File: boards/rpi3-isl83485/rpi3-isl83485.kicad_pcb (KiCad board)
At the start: 2 copper layers, 24.8 x 15.2 mm, 9 parts, among them J1 RPi, J2 JST-GH, U1 ISL83485

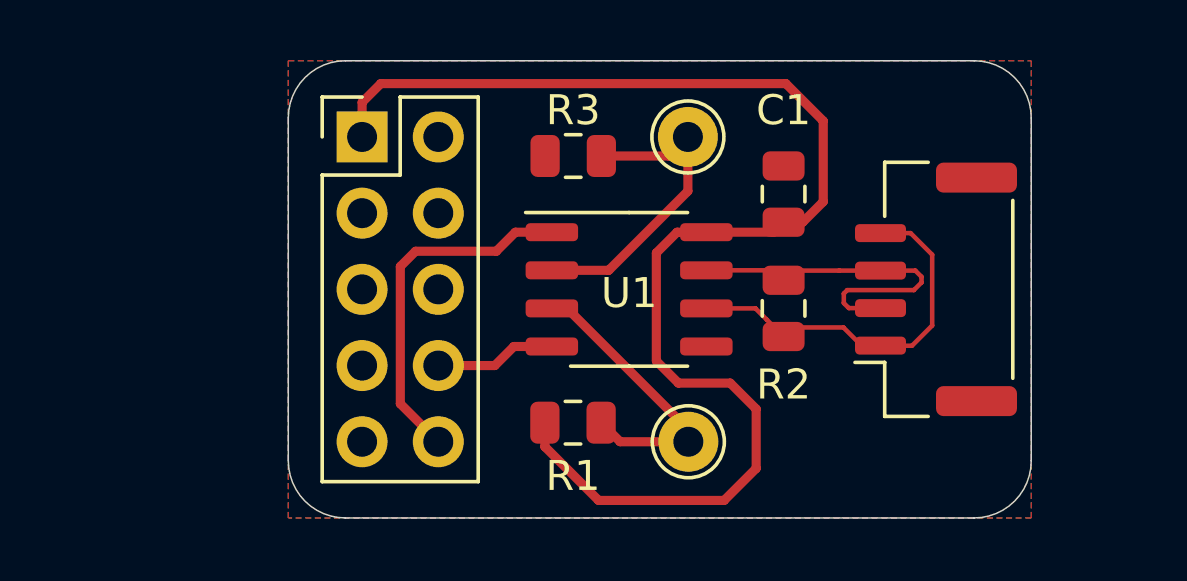
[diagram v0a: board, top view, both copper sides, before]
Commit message: No longer interested in ISL83488.
Layout for ICE40HX8K-BG121 -- just need power.
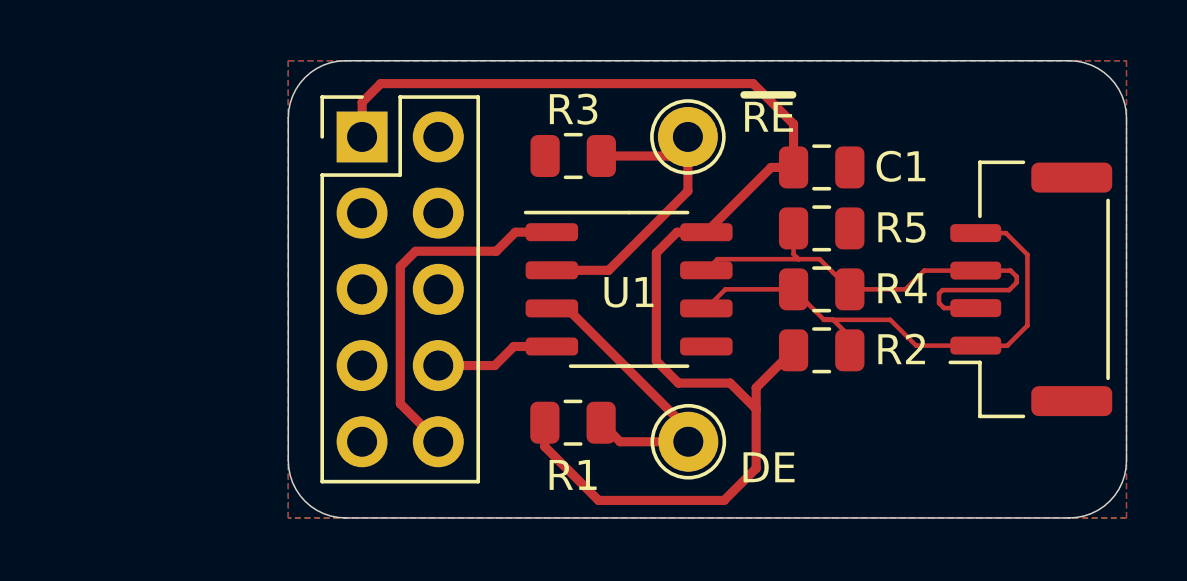
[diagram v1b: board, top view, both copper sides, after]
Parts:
- added R4: Rt, Resistor_SMD:R_0805_2012Metric, F.Cu at (34.3, 22.9)
- added R5: Rb, Resistor_SMD:R_0805_2012Metric, F.Cu at (34.3, 20.8)
- R2: value 100R -> Rb
- moved J2 3.17 mm to (41.3, 22.9)
- moved R2 1.89 mm to (34.3, 24.9), turned to 0 degrees
- moved C1 1.55 mm to (34.3, 18.8), turned to 0 degrees
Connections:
- R2 pad 1: /DS- -> +3V3
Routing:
- net /DS+: track 13.0 -> 18.0 mm
- net /DS-: track 12.1 -> 16.9 mm
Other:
- board size 24.8 x 15.2 mm -> 27.9 x 15.2 mm
- board text added: "DE"
- board text added: "rpi3-isl83485 fourside.io"
- board text added: "~RE"

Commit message: Send to fab.
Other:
- outline, holes or cut-outs redrawn
- board text added: "rpi3<>isl83485 fourside.io"
- board text removed: "rpi3-isl83485 fourside.io"
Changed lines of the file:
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@@
   (page A4)
   (layers
-    (0 F.Cu signal)
-    (31 B.Cu signal)
+    (0 F.Cu signal hide)
+    (31 B.Cu signal hide)
     (32 B.Adhes user hide)
     (33 F.Adhes user hide)
@@
   )
   (setup
-    (last_trace_width 0.1524)
+    (last_trace_width 0.25)
     (user_trace_width 0.1016)
     (user_trace_width 0.1524)
@@
       (usegerberextensions false)
       (usegerberattributes false)
-      (usegerberadvancedattributes false)
+      (usegerberadvancedattributes true)
       (creategerberjobfile false)
-      (excludeedgelayer true)
-      (linewidth 0.100000)
+      (excludeedgelayer false)
+      (linewidth 0.150000)
       (plotframeref false)
       (viasonmask false)
       (mode 1)
-      (useauxorigin false)
+      (useauxorigin true)
       (hpglpennumber 1)
       (hpglpenspeed 20)
@@
       (psa4output false)
       (plotreference true)
-      (plotvalue true)
+      (plotvalue false)
       (plotinvisibletext false)
       (padsonsilk false)
-      (subtractmaskfromsilk false)
+      (subtractmaskfromsilk true)
       (outputformat 1)
       (mirror false)
-      (drillshape 1)
+      (drillshape 0)
       (scaleselection 1)
-      (outputdirectory ""))
+      (outputdirectory "gerbers/"))
   )
   (net 0 "")
@@
     (pad 8 smd roundrect (at 2.575 -1.905) (size 1.75 0.6) (layers F.Cu F.Paste F.Mask) (roundrect_rratio 0.25)
       (net 2 +3V3))
-    (model ${KISYS3DMOD}/Package_SO.3dshapes/SO-8_3.9x4.9mm_P1.27mm.wrl
+    (model ${KISYS3DMOD}/Package_SO.3dshapes/HSOP-8-1EP_3.9x4.9mm_P1.27mm_EP2.41x3.1mm.wrl
       (at (xyz 0 0 0))
       (scale (xyz 1 1 1))
@@
     )
   )
-  (gr_text "rpi3-isl83485\nfourside.io" (at 43.561 22.86) (layer B.Mask)
+  (gr_arc (start 43.18 29.21) (end 43.18 30.48) (angle -90) (layer Edge.Cuts) (width 0.05))
+  (gr_arc (start 17.78 29.21) (end 16.51 29.21) (angle -90) (layer Edge.Cuts) (width 0.05))
+  (gr_arc (start 17.78 16.51) (end 17.78 15.24) (angle -90) (layer Edge.Cuts) (width 0.05))
+  (gr_arc (start 43.18 16.51) (end 44.45 16.51) (angle -90) (layer Edge.Cuts) (width 0.05))
+  (gr_text "rpi3<>isl83485\nfourside.io" (at 43.561 22.86) (layer B.Mask)
     (effects (font (size 1.5 1.5) (thickness 0.3)) (justify left mirror))
   )
@@
     (effects (font (size 1 1) (thickness 0.25)))
   )
-  (gr_arc (start 18.415 28.575) (end 16.51 28.575) (angle -90) (layer Edge.Cuts) (width 0.05))
-  (gr_arc (start 18.415 17.145) (end 18.415 15.24) (angle -90) (layer Edge.Cuts) (width 0.05))
-  (gr_arc (start 42.545 28.575) (end 42.545 30.48) (angle -90) (layer Edge.Cuts) (width 0.05))
-  (gr_arc (start 42.545 17.145) (end 44.45 17.145) (angle -90) (layer Edge.Cuts) (width 0.05))
-  (gr_line (start 16.51 28.575) (end 16.51 17.145) (layer Edge.Cuts) (width 0.05))
-  (gr_line (start 42.545 30.48) (end 18.415 30.48) (layer Edge.Cuts) (width 0.05))
-  (gr_line (start 44.45 17.145) (end 44.45 28.575) (layer Edge.Cuts) (width 0.05))
-  (gr_line (start 18.415 15.24) (end 42.545 15.24) (layer Edge.Cuts) (width 0.05))
+  (gr_line (start 16.51 29.21) (end 16.51 16.51) (layer Edge.Cuts) (width 0.05))
+  (gr_line (start 43.18 30.48) (end 17.78 30.48) (layer Edge.Cuts) (width 0.05))
+  (gr_line (start 44.45 16.51) (end 44.45 29.21) (layer Edge.Cuts) (width 0.05))
+  (gr_line (start 17.78 15.24) (end 43.18 15.24) (layer Edge.Cuts) (width 0.05))
   (segment (start 29.47 20.955) (end 30.445 20.955) (width 0.3048) (layer F.Cu) (net 2))
   (segment (start 28.7782 21.6468) (end 29.47 20.955) (width 0.3048) (layer F.Cu) (net 2))

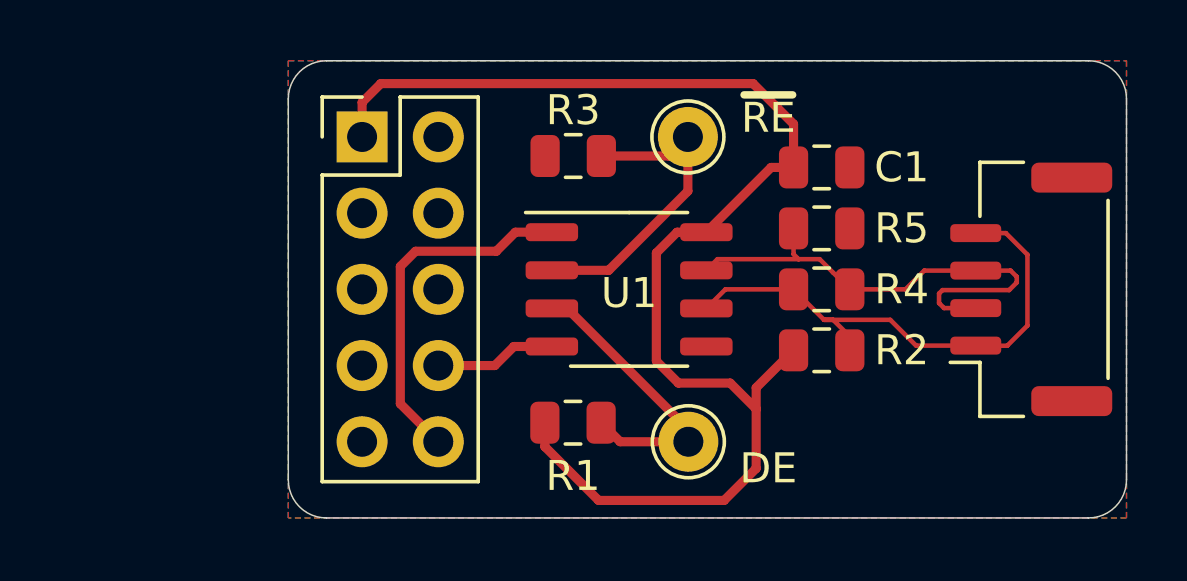
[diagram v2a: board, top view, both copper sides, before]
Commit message: For whatever reason, updated ISL83485.
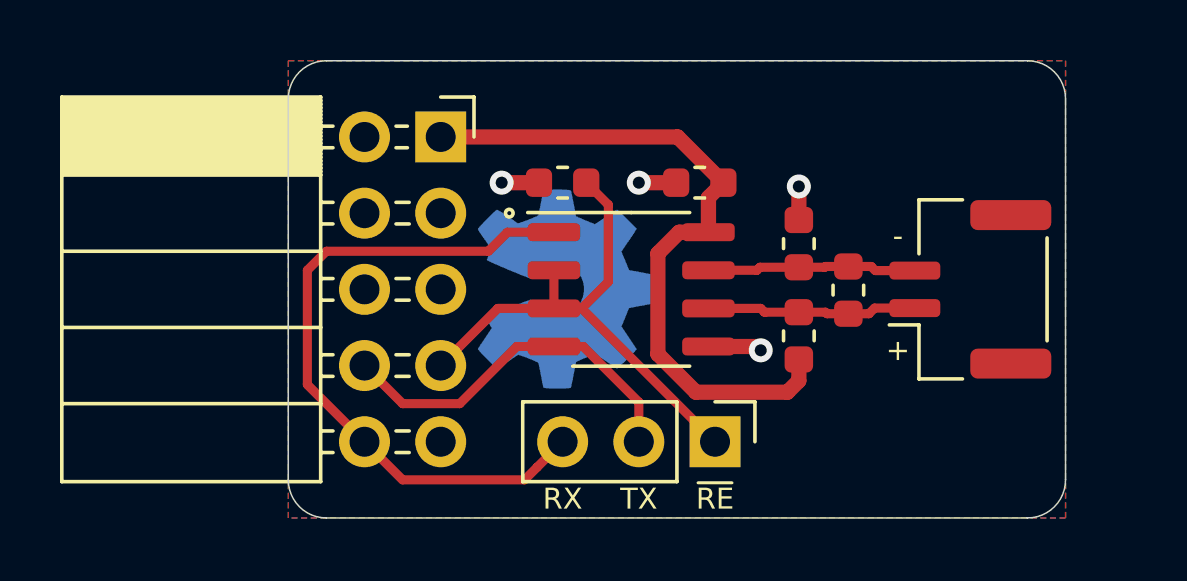
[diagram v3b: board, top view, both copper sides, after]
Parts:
- removed R1: 4k7, Resistor_SMD:R_0805_2012Metric
- removed TP1: ~RE, TestPoint:TestPoint_THTPad_D2.0mm_Drill1.0mm
- removed TP2: DE, TestPoint:TestPoint_THTPad_D2.0mm_Drill1.0mm
- added J3: JST-GH, Connector_JST:JST_GH_SM02B-GHS-TB_1x02-1MP_P1.25mm_Horizontal, F.Cu at (39.2, 22.9)
- added REF**: OSHW-Symbol_6.7x6mm_Copper, Symbol:OSHW-Symbol_6.7x6mm_Copper, B.Cu at (25.8, 22.9)
- C1: footprint Capacitor_SMD:C_0805_2012Metric -> Capacitor_SMD:C_0603_1608Metric
- J1: footprint Connector_PinHeader_2.54mm:PinHeader_2x05_P2.54mm_Vertical -> Connector_PinSocket_2.54mm:PinSocket_2x05_P2.54mm_Horizontal
- J2: value JST-GH -> Conn_01x03; footprint Connector_JST:JST_GH_SM04B-GHS-TB_1x04-1MP_P1.25mm_Horizontal -> Connector_PinHeader_2.54mm:PinHeader_1x03_P2.54mm_Vertical
- R2, R4, R5: footprint Resistor_SMD:R_0805_2012Metric -> Resistor_SMD:R_0603_1608Metric
- R3: value 4k7 -> 10k; footprint Resistor_SMD:R_0805_2012Metric -> Resistor_SMD:R_0603_1608Metric
- moved J2 11.7 mm to (30.7, 27.9), turned to 270 degrees
- moved C1 4.10 mm to (30.2, 19.3), turned to 180 degrees
- moved J1 2.62 mm to (21.6, 17.8)
- moved R3 0.96 mm to (25.7, 19.3)
- moved R5 0.92 mm to (33.5, 21.3), turned to 90 degrees
- moved R2 0.90 mm to (33.5, 24.4), turned to 90 degrees
- moved R4 0.89 mm to (35.2, 22.9), turned to 90 degrees
- moved U1 0.07 mm to (27.9, 22.9)
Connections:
- J1 pad 7: Net-(J1-Pad7) -> /~RE
- J2 pad 1: /DS+ -> /~RE
- J2 pad 2: /DS- -> /TxD
- J2 pad 3: /DS- -> /RxD
- U1 pad 3: /DE -> /~RE
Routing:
- net +3V3: track 44.6 -> 23.3 mm
- net /RxD: track 11.9 -> 22.9 mm
- net /DS+: track 18.0 -> 7.03 mm
- net /DS-: track 16.9 -> 6.99 mm
- net /DE: track 9.82 -> 0.00 mm
- net /TxD: track 4.05 -> 12.5 mm
- net /~RE: track 10.6 -> 17.9 mm
- net GND: track 0.00 -> 5.40 mm, vias 0 -> 4
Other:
- board size 27.9 x 15.2 mm -> 25.9 x 15.2 mm
- board text added: "+"
- board text added: "-"
- board text added: "RX"
- board text added: "TX"
- board text added: "rpi-isl83485 2020-01 fourside.io"
- board text removed: "DE"
- board text removed: "rpi3<>isl83485 fourside.io"
